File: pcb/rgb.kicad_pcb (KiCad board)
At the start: 2 copper layers, 58 x 48 mm, 73 parts, among them J1 2.54-2*8P, J3 B4PS-VH, J4 TYPE-C-31-M-12, J5 TF-01A, J6 V_BATT, J7 B4PS-VH, SW1 MS-22C01-G010, U1 SY8286ARAC, U11 RV-3028-C7, U2 SY8286ARAC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

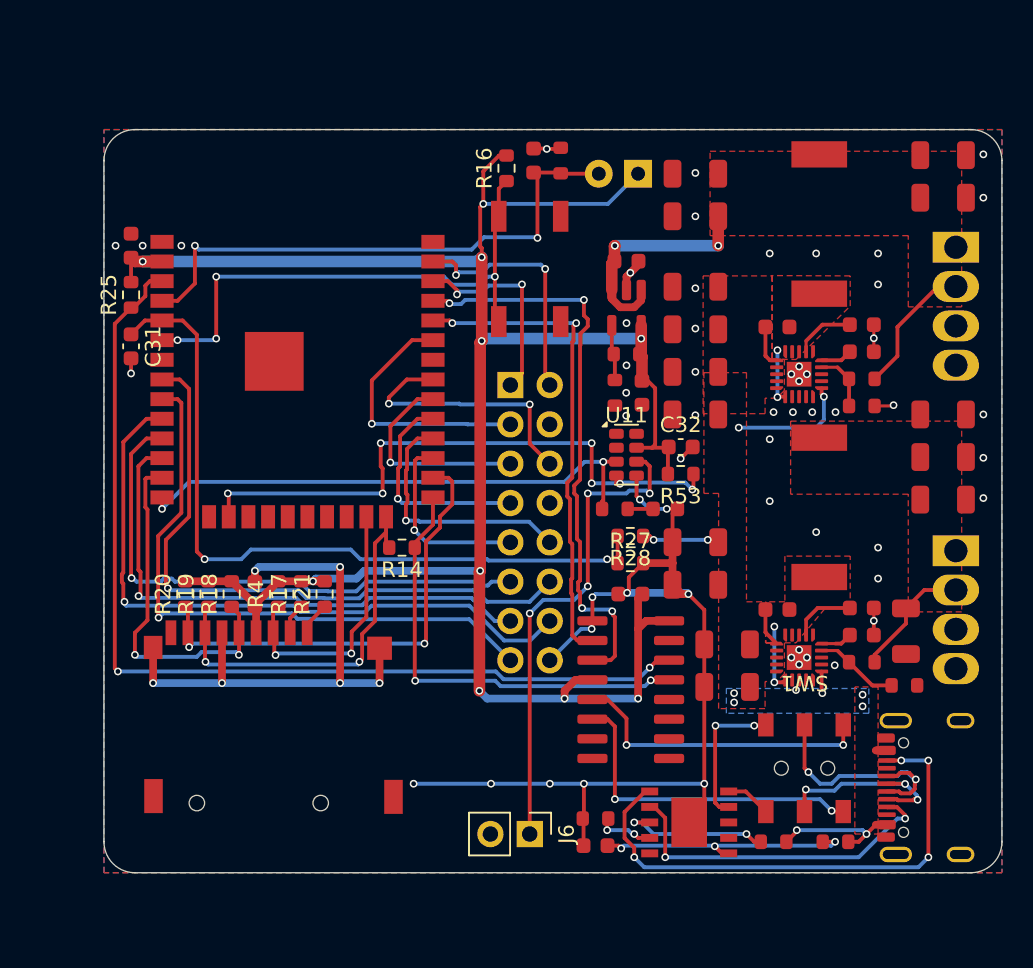
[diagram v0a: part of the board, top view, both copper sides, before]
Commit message: rev3 pcb: add IR receiver
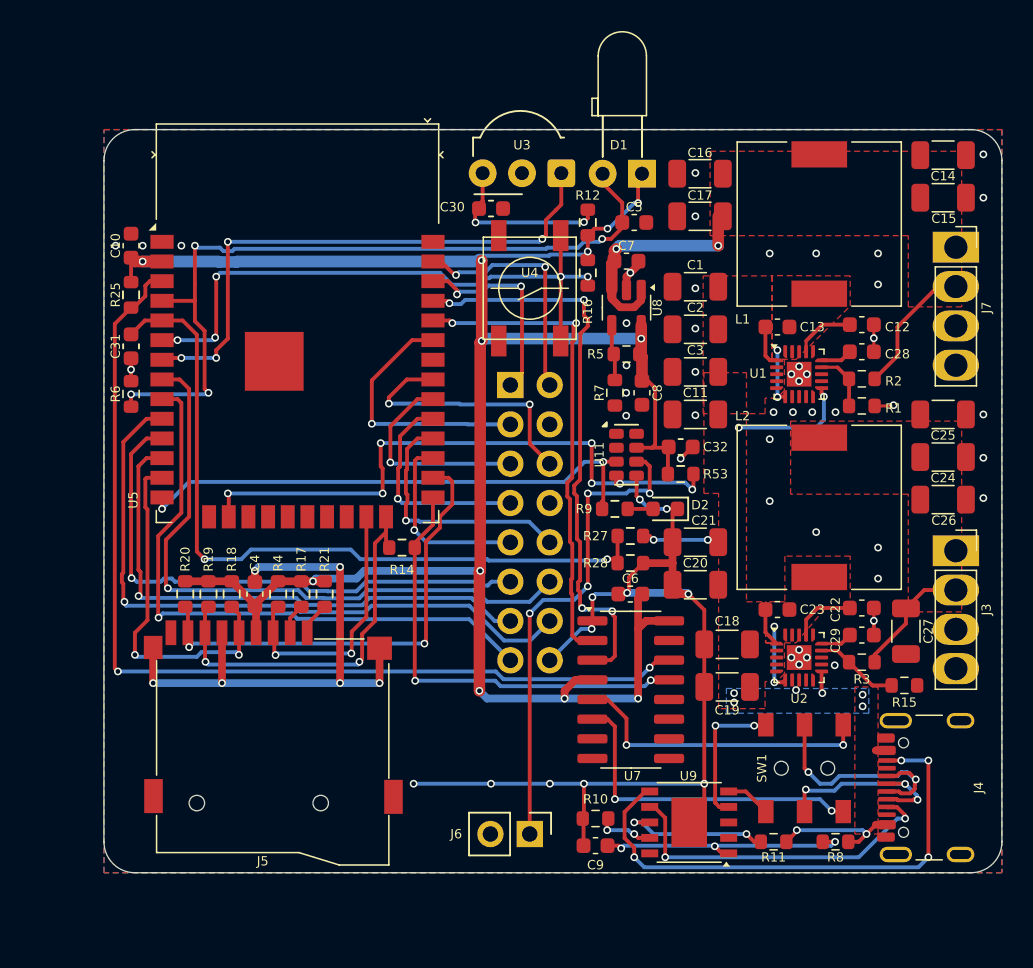
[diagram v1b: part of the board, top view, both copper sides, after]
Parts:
- added C30: 2u2, Capacitor_SMD:C_0603_1608Metric, F.Cu at (69.0, 80.1)
- added R12: 100R, Resistor_SMD:R_0603_1608Metric, F.Cu at (75.2, 81.0)
- added U3: IRM-56384, OptoDevice:Vishay_MOLD-3Pin, F.Cu at (73.5, 77.8)
- moved R6 31.6 mm to (45.8, 92.1)
- moved R16 8.55 mm to (75.2, 84.2)
- moved C5 7.63 mm to (78.2, 81.0), turned to 0 degrees
- moved U4 1.25 mm to (71.5, 85.2), turned to -90 degrees
- moved C16 0.30 mm to (82.5, 77.8)
- moved C17 0.30 mm to (82.5, 80.6)
- moved D1 0.25 mm to (78.8, 77.8)
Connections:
- U5 pad 7: unconnected-(U5-IO35-Pad7) -> Net-(U3-OUT)
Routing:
- net Net-(U3-OUT): track 0.00 -> 36.5 mm, vias 0 -> 4
- net Net-(D1-A): track 36.1 -> 50.2 mm, vias 2 -> 4
- net Net-(U3-Vs): track 0.00 -> 11.4 mm, vias 0 -> 2
- net Net-(U5-IO34): track 35.5 -> 39.6 mm, vias 4 -> 5
- net +3.3V: track 141.1 -> 137.3 mm, vias 10 -> 12
- net GND: track 112.9 -> 111.8 mm, vias 65 -> 64

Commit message: pcb: remove D1 data pin from SD card
  * 2 wire MMC mode does not exist. Can only use 1 wire anyway.
  * Use the freed up GPIO for address line E
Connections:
- J5 pad 8: /SD_D1 -> Net-(J5-DAT1)
- R20 pad 1: /SD_D1 -> Net-(J5-DAT1)
- U5 pad 26: /SD_D1 -> /E
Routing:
- net /SD_D1: track 30.6 -> 0.00 mm, vias 2 -> 0
- net /E: track 0.00 -> 11.0 mm, vias 0 -> 2
- net Net-(J5-DAT1): track 0.00 -> 1.75 mm
- net /USB_N: track 13.1 -> 14.4 mm
- net /USB_N_S: track 21.4 -> 22.2 mm
- net /A: track 12.3 -> 12.9 mm
- net /R1: track 13.6 -> 14.2 mm

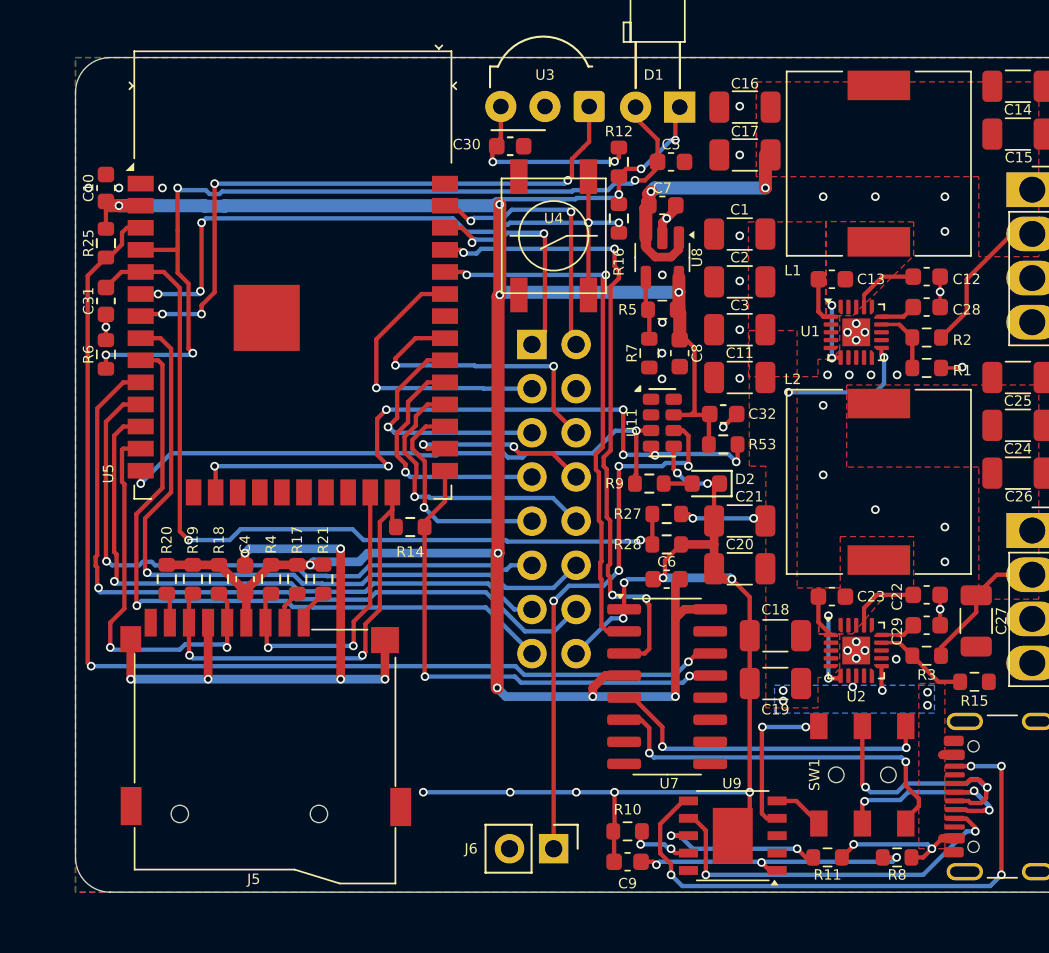
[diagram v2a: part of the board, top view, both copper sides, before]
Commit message: pcb: optimize GND plane
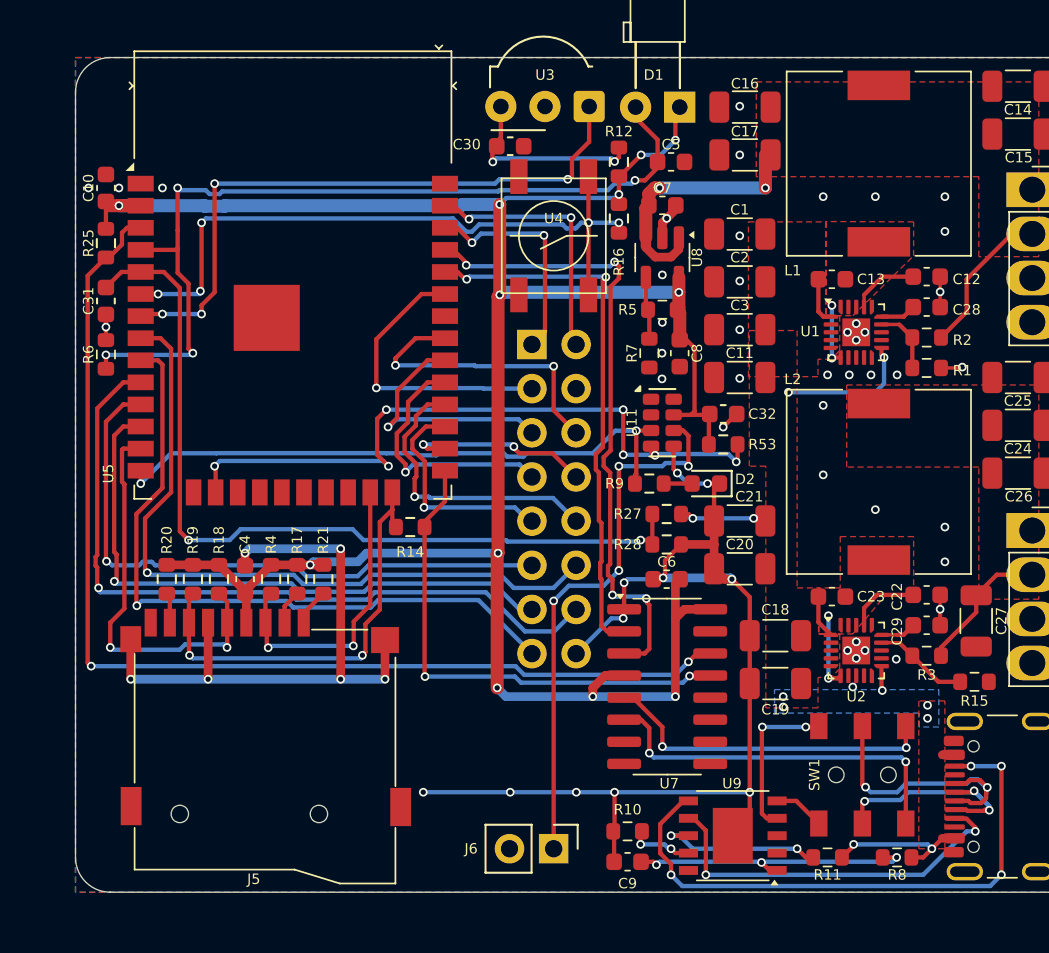
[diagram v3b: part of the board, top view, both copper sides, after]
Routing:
- net /USB_N_S: track 22.2 -> 21.6 mm
- net /G0: track 15.7 -> 15.1 mm
